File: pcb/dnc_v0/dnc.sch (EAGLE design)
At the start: 17 parts, among them IC1 74HC595D, IC2 74HC595D, Q1 MOSFET-NCHANNEL_DUALFDMA1024NZ, U1 ATMEGA168, Y1 16MHZ

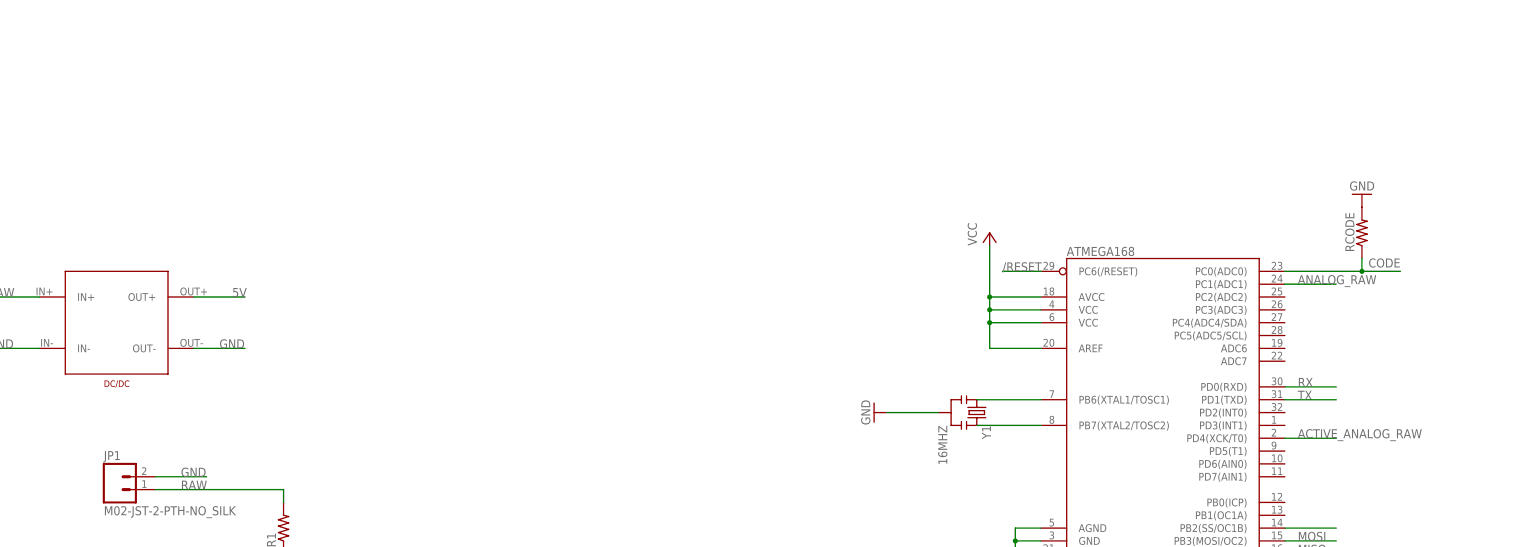
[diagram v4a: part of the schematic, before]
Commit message: Add Temp sensor and two 74HC595 for titreur select
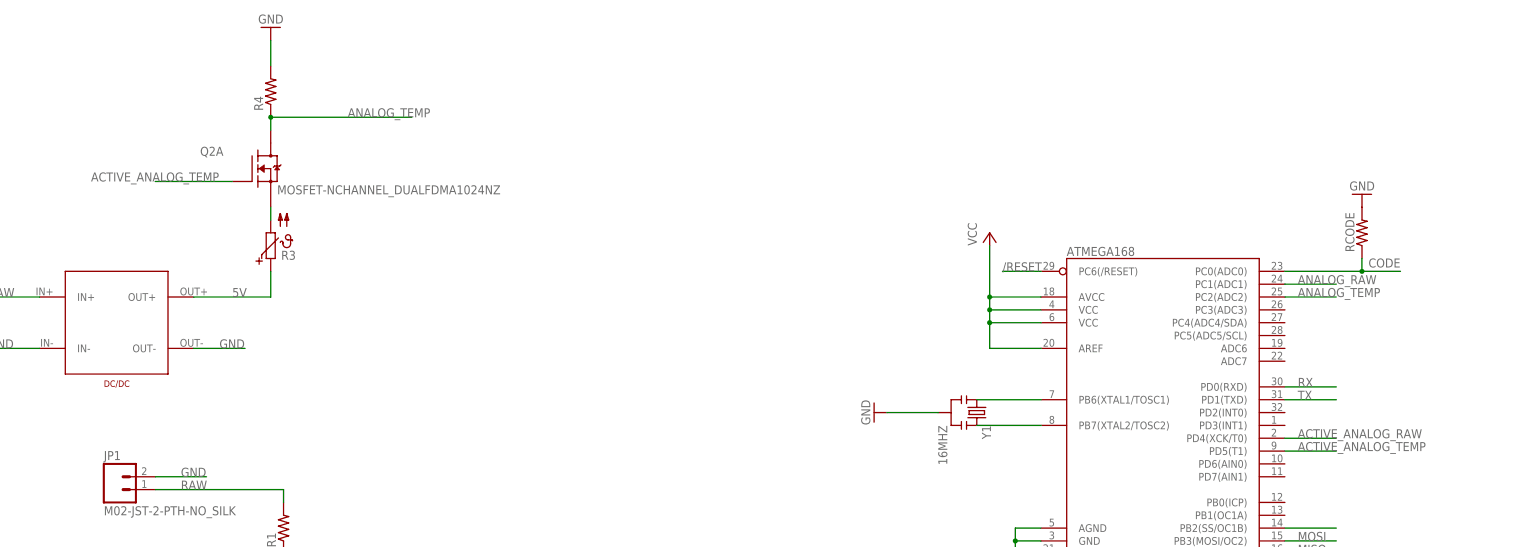
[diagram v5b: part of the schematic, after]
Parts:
- added Q2: MOSFET-NCHANNEL_DUALFDMA1024NZ, SparkFun-DiscreteSemi:MOSFET-NCHANNEL_DUALFDMA1024NZ
- added R3: (no value), ptc-ntc:PTC679
- added R4: (no value), SparkFun-Passives:RESISTOR1206
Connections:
- new net ACTIVE_ANALOG_TEMP: Q2A.G, U1.PD5(T1)
- new net ANALOG_TEMP: Q2A.D1, R4.1, U1.PC2(ADC2)
- new net N$11: Q2A.S, R3.2
- net 5V: now also R3.1
- net GND: now also R4.2
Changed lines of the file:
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@@
 <part name="U$7" library="pierre_vv" deviceset="EXT-DNC" device=""/>
 <part name="U$8" library="pierre_vv" deviceset="EXT-DNC" device=""/>
+<part name="R3" library="ptc-ntc" deviceset="PTC679" device=""/>
+<part name="R4" library="SparkFun-Passives" deviceset="RESISTOR" device="1206"/>
+<part name="GND3" library="SparkFun-Aesthetics" deviceset="GND" device=""/>
+<part name="Q2" library="SparkFun-DiscreteSemi" deviceset="MOSFET-NCHANNEL_DUAL" device="FDMA1024NZ"/>
 </parts>
 <sheets>
@@
 <instance part="U$7" gate="G$1" x="-45.72" y="-180.34"/>
 <instance part="U$8" gate="G$1" x="-45.72" y="-203.2"/>
+<instance part="R3" gate="1" x="-132.08" y="109.22"/>
+<instance part="R4" gate="G$1" x="-132.08" y="139.7" rot="R90"/>
+<instance part="GND3" gate="1" x="-132.08" y="152.4" rot="R180"/>
+<instance part="Q2" gate="A" x="-134.62" y="124.46"/>
 </instances>
 <busses>
@@
 <wire x1="-40.64" y1="-195.58" x2="-7.62" y2="-195.58" width="0.1524" layer="91"/>
 <label x="-15.24" y="-195.58" size="1.778" layer="95"/>
+</segment>
+<segment>
+<pinref part="R4" gate="G$1" pin="2"/>
+<pinref part="GND3" gate="1" pin="GND"/>
+<wire x1="-132.08" y1="144.78" x2="-132.08" y2="149.86" width="0.1524" layer="91"/>
 </segment>
 </net>
@@
 <segment>
 <pinref part="U$5" gate="G$1" pin="OUT+"/>
-<wire x1="-147.32" y1="99.06" x2="-137.16" y2="99.06" width="0.1524" layer="91"/>
+<wire x1="-147.32" y1="99.06" x2="-132.08" y2="99.06" width="0.1524" layer="91"/>
 <label x="-139.7" y="99.06" size="1.778" layer="95"/>
+<pinref part="R3" gate="1" pin="1"/>
+<wire x1="-132.08" y1="99.06" x2="-132.08" y2="104.14" width="0.1524" layer="91"/>
 </segment>
 </net>
@@
 </segment>
 </net>
+<net name="N$11" class="0">
+<segment>
+<pinref part="R3" gate="1" pin="2"/>
+<pinref part="Q2" gate="A" pin="S"/>
+<wire x1="-132.08" y1="114.3" x2="-132.08" y2="116.84" width="0.1524" layer="91"/>
+</segment>
+</net>
+<net name="ANALOG_TEMP" class="0">
+<segment>
+<pinref part="Q2" gate="A" pin="D1"/>
+<pinref part="R4" gate="G$1" pin="1"/>
+<wire x1="-132.08" y1="132.08" x2="-132.08" y2="134.62" width="0.1524" layer="91"/>
+<wire x1="-132.08" y1="134.62" x2="-104.14" y2="134.62" width="0.1524" layer="91"/>
+<junction x="-132.08" y="134.62"/>
+<label x="-116.84" y="134.62" size="1.778" layer="95"/>
+</segment>
+<segment>
+<pinref part="U1" gate="G$1" pin="PC2(ADC2)"/>
+<wire x1="68.58" y1="99.06" x2="78.74" y2="99.06" width="0.1524" layer="91"/>
+<label x="71.12" y="99.06" size="1.778" layer="95"/>
+</segment>
+</net>
+<net name="ACTIVE_ANALOG_TEMP" class="0">
+<segment>
+<pinref part="Q2" gate="A" pin="G"/>
+<wire x1="-139.7" y1="121.92" x2="-154.94" y2="121.92" width="0.1524" layer="91"/>
+<label x="-167.64" y="121.92" size="1.778" layer="95"/>
+</segment>
+<segment>
+<pinref part="U1" gate="G$1" pin="PD5(T1)"/>
+<wire x1="68.58" y1="68.58" x2="78.74" y2="68.58" width="0.1524" layer="91"/>
+<label x="71.12" y="68.58" size="1.778" layer="95"/>
+</segment>
+</net>

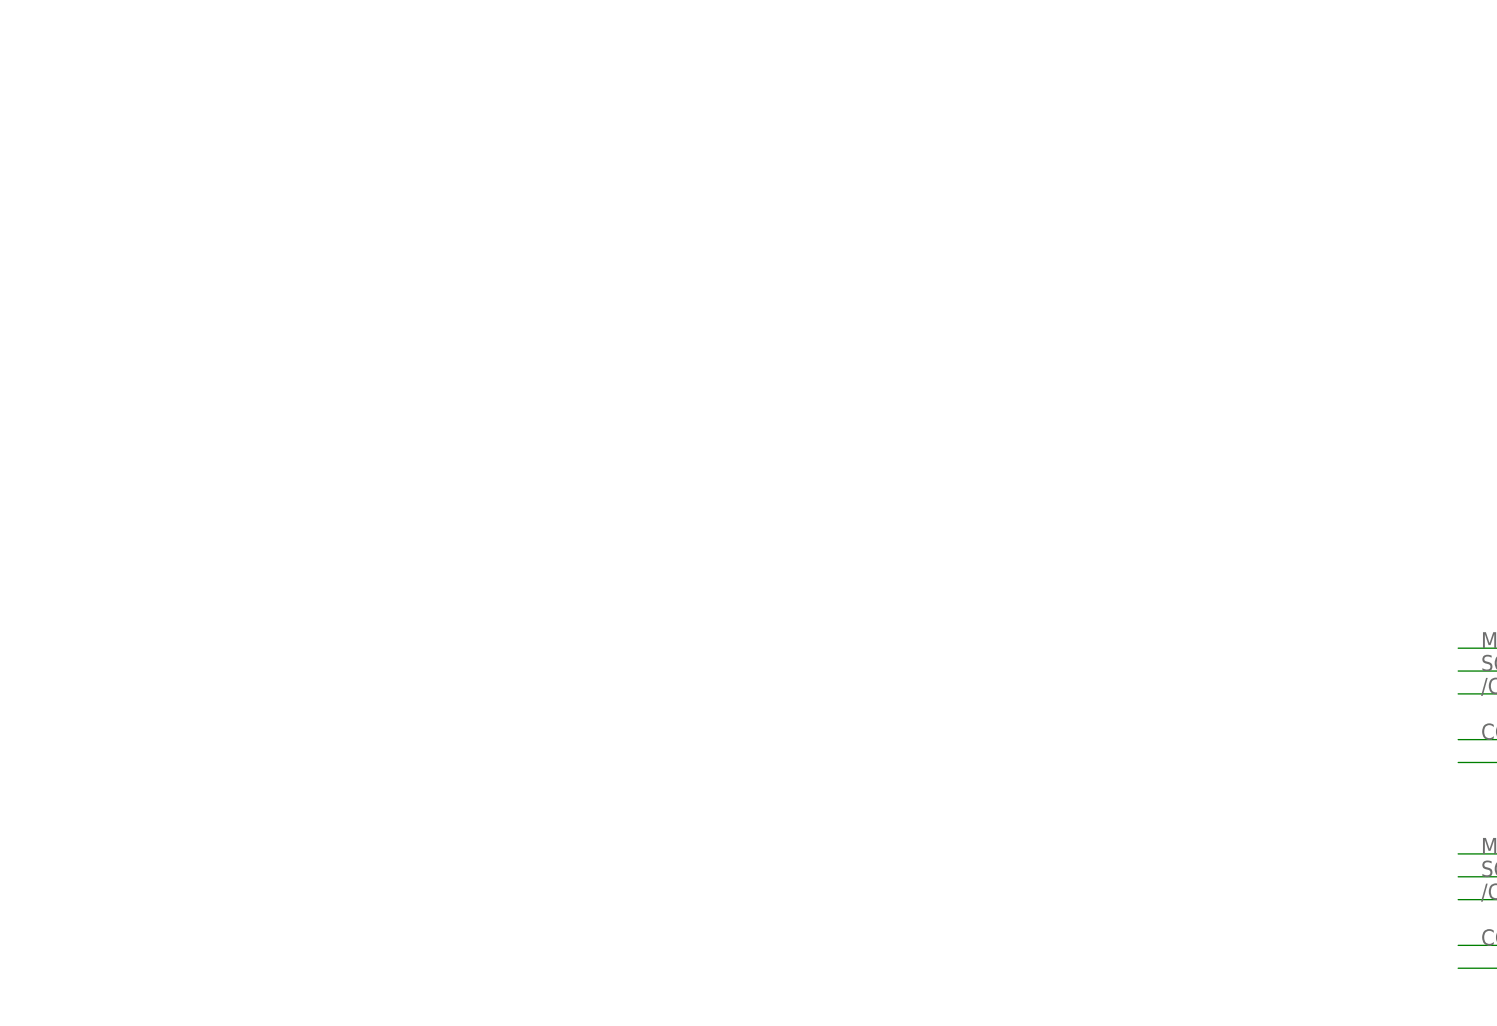
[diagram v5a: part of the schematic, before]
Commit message: Add 3 power output (ugly)
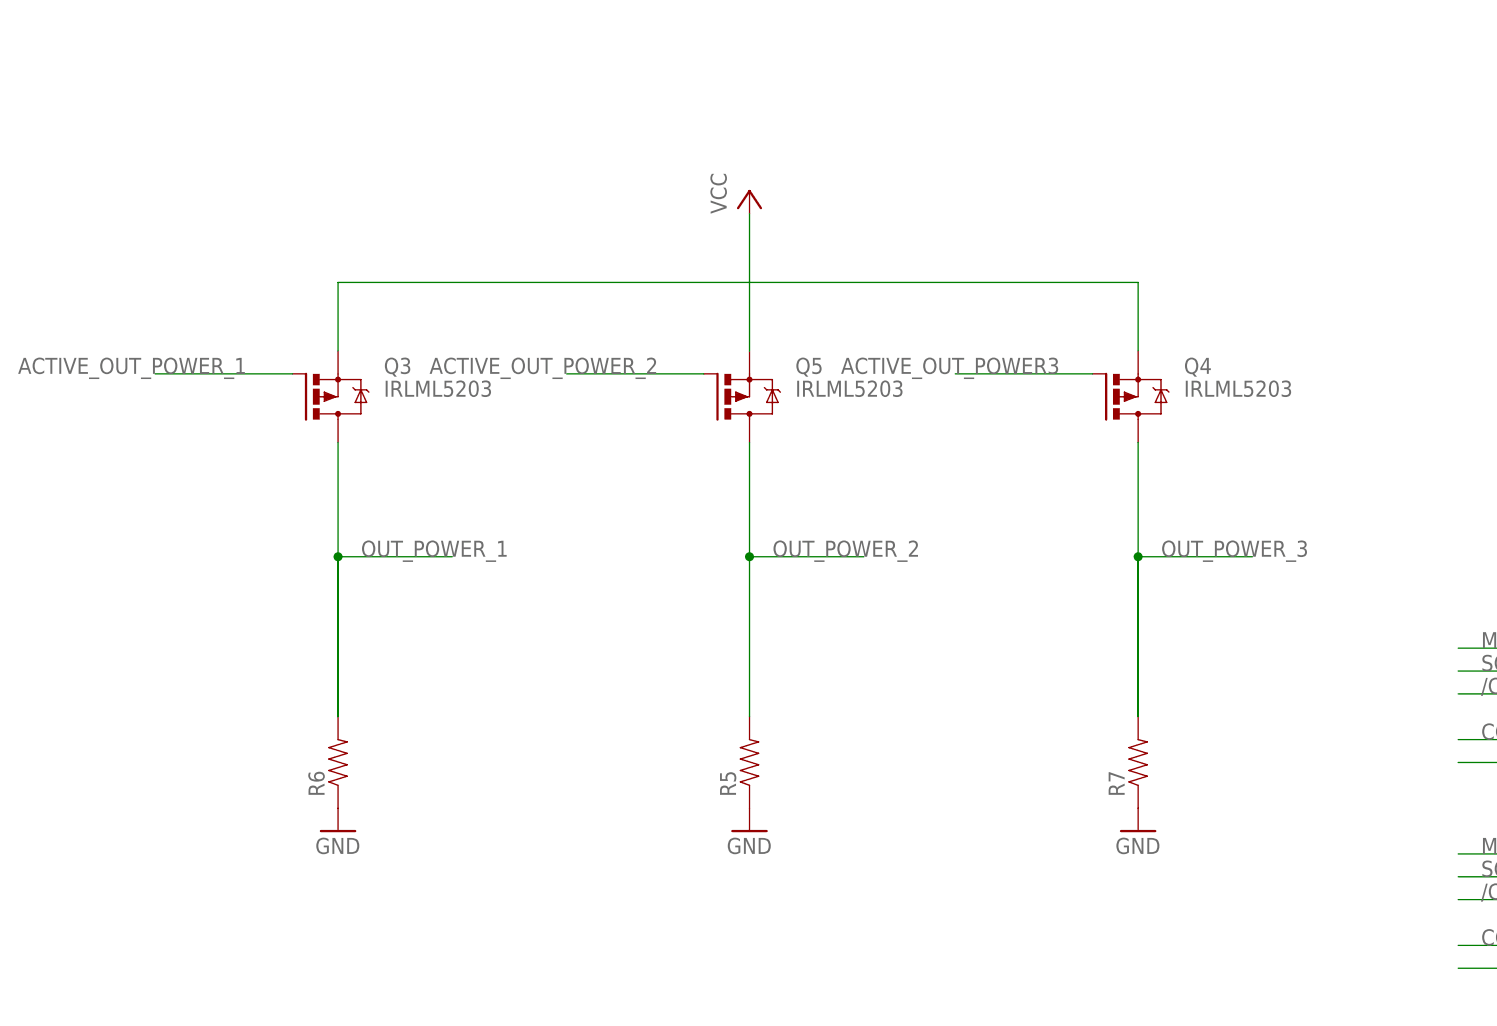
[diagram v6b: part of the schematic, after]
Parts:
- added Q3, Q4, Q5: IRLML5203, transistor-power:IRLML5203
- added R5, R6, R7: (no value), SparkFun-Passives:RESISTOR1206
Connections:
- new net ACTIVE_OUT_POWER3: Q4.G
- new net ACTIVE_OUT_POWER_1: Q3.G
- new net ACTIVE_OUT_POWER_2: Q5.G
- new net N$12: Q3.S, Q4.S
- new net N$26: R6.2
- new net N$29: R7.2
- new net OUT_POWER_1: Q3.D
- new net OUT_POWER_2: Q5.D, R5.2
- new net OUT_POWER_3: Q4.D
- net GND: now also R5.1, R6.1, R7.1
- net VCC: now also Q5.S
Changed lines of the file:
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@@
 <part name="GND3" library="SparkFun-Aesthetics" deviceset="GND" device=""/>
 <part name="Q2" library="SparkFun-DiscreteSemi" deviceset="MOSFET-NCHANNEL_DUAL" device="FDMA1024NZ"/>
+<part name="Q3" library="transistor-power" deviceset="IRLML5203" device=""/>
+<part name="Q4" library="transistor-power" deviceset="IRLML5203" device=""/>
+<part name="Q5" library="transistor-power" deviceset="IRLML5203" device=""/>
+<part name="R5" library="SparkFun-Passives" deviceset="RESISTOR" device="1206"/>
+<part name="GND4" library="SparkFun-Aesthetics" deviceset="GND" device=""/>
+<part name="P+3" library="supply1" deviceset="VCC" device=""/>
+<part name="R6" library="SparkFun-Passives" deviceset="RESISTOR" device="1206"/>
+<part name="GND7" library="SparkFun-Aesthetics" deviceset="GND" device=""/>
+<part name="R7" library="SparkFun-Passives" deviceset="RESISTOR" device="1206"/>
+<part name="GND8" library="SparkFun-Aesthetics" deviceset="GND" device=""/>
 </parts>
 <sheets>
@@
 <instance part="GND3" gate="1" x="-132.08" y="152.4" rot="R180"/>
 <instance part="Q2" gate="A" x="-134.62" y="124.46"/>
+<instance part="Q3" gate="G$1" x="-218.44" y="-48.26"/>
+<instance part="Q4" gate="G$1" x="-129.54" y="-48.26"/>
+<instance part="Q5" gate="G$1" x="-172.72" y="-48.26"/>
+<instance part="R5" gate="G$1" x="-170.18" y="-88.9" rot="R90"/>
+<instance part="GND4" gate="1" x="-170.18" y="-96.52"/>
+<instance part="P+3" gate="VCC" x="-170.18" y="-25.4"/>
+<instance part="R6" gate="G$1" x="-215.9" y="-88.9" rot="R90"/>
+<instance part="GND7" gate="1" x="-215.9" y="-96.52"/>
+<instance part="R7" gate="G$1" x="-127" y="-88.9" rot="R90"/>
+<instance part="GND8" gate="1" x="-127" y="-96.52"/>
 </instances>
 <busses>
@@
 <pinref part="GND3" gate="1" pin="GND"/>
 <wire x1="-132.08" y1="144.78" x2="-132.08" y2="149.86" width="0.1524" layer="91"/>
+</segment>
+<segment>
+<pinref part="R5" gate="G$1" pin="1"/>
+<pinref part="GND4" gate="1" pin="GND"/>
+</segment>
+<segment>
+<pinref part="R6" gate="G$1" pin="1"/>
+<pinref part="GND7" gate="1" pin="GND"/>
+</segment>
+<segment>
+<pinref part="R7" gate="G$1" pin="1"/>
+<pinref part="GND8" gate="1" pin="GND"/>
 </segment>
 </net>
@@
 <label x="-15.24" y="-190.5" size="1.778" layer="95"/>
 </segment>
+<segment>
+<pinref part="P+3" gate="VCC" pin="VCC"/>
+<pinref part="Q5" gate="G$1" pin="S"/>
+<wire x1="-170.18" y1="-43.18" x2="-170.18" y2="-27.94" width="0.1524" layer="91"/>
+</segment>
 </net>
 <net name="MOSI" class="0">
@@
 </segment>
 </net>
+<net name="N$12" class="0">
+<segment>
+<pinref part="Q3" gate="G$1" pin="S"/>
+<wire x1="-215.9" y1="-43.18" x2="-215.9" y2="-35.56" width="0.1524" layer="91"/>
+<wire x1="-215.9" y1="-35.56" x2="-127" y2="-35.56" width="0.1524" layer="91"/>
+<pinref part="Q4" gate="G$1" pin="S"/>
+<wire x1="-127" y1="-35.56" x2="-127" y2="-43.18" width="0.1524" layer="91"/>
+</segment>
+</net>
+<net name="OUT_POWER_1" class="0">
+<segment>
+<pinref part="Q3" gate="G$1" pin="D"/>
+<wire x1="-215.9" y1="-53.34" x2="-215.9" y2="-66.04" width="0.1524" layer="91"/>
+<wire x1="-215.9" y1="-66.04" x2="-215.9" y2="-83.82" width="0.1524" layer="91"/>
+<junction x="-215.9" y="-66.04"/>
+<wire x1="-215.9" y1="-66.04" x2="-203.2" y2="-66.04" width="0.1524" layer="91"/>
+<label x="-213.36" y="-66.04" size="1.778" layer="95"/>
+</segment>
+</net>
+<net name="ACTIVE_OUT_POWER_1" class="0">
+<segment>
+<pinref part="Q3" gate="G$1" pin="G"/>
+<wire x1="-220.98" y1="-45.72" x2="-236.22" y2="-45.72" width="0.1524" layer="91"/>
+<label x="-251.46" y="-45.72" size="1.778" layer="95"/>
+</segment>
+</net>
+<net name="ACTIVE_OUT_POWER_2" class="0">
+<segment>
+<pinref part="Q5" gate="G$1" pin="G"/>
+<wire x1="-175.26" y1="-45.72" x2="-190.5" y2="-45.72" width="0.1524" layer="91"/>
+<label x="-205.74" y="-45.72" size="1.778" layer="95"/>
+</segment>
+</net>
+<net name="ACTIVE_OUT_POWER3" class="0">
+<segment>
+<pinref part="Q4" gate="G$1" pin="G"/>
+<wire x1="-132.08" y1="-45.72" x2="-147.32" y2="-45.72" width="0.1524" layer="91"/>
+<label x="-160.02" y="-45.72" size="1.778" layer="95"/>
+</segment>
+</net>
+<net name="OUT_POWER_2" class="0">
+<segment>
+<pinref part="R5" gate="G$1" pin="2"/>
+<pinref part="Q5" gate="G$1" pin="D"/>
+<wire x1="-170.18" y1="-53.34" x2="-170.18" y2="-66.04" width="0.1524" layer="91"/>
+<wire x1="-170.18" y1="-66.04" x2="-157.48" y2="-66.04" width="0.1524" layer="91"/>
+<junction x="-170.18" y="-66.04"/>
+<wire x1="-170.18" y1="-66.04" x2="-170.18" y2="-83.82" width="0.1524" layer="91"/>
+<label x="-167.64" y="-66.04" size="1.778" layer="95"/>
+</segment>
+</net>
+<net name="N$26" class="0">
+<segment>
+<pinref part="R6" gate="G$1" pin="2"/>
+<wire x1="-215.9" y1="-66.04" x2="-215.9" y2="-83.82" width="0.1524" layer="91"/>
+</segment>
+</net>
+<net name="N$29" class="0">
+<segment>
+<pinref part="R7" gate="G$1" pin="2"/>
+<wire x1="-127" y1="-66.04" x2="-127" y2="-83.82" width="0.1524" layer="91"/>
+</segment>
+</net>
+<net name="OUT_POWER_3" class="0">
+<segment>
+<pinref part="Q4" gate="G$1" pin="D"/>
+<wire x1="-127" y1="-83.82" x2="-127" y2="-66.04" width="0.1524" layer="91"/>
+<wire x1="-127" y1="-66.04" x2="-127" y2="-53.34" width="0.1524" layer="91"/>
+<wire x1="-127" y1="-66.04" x2="-114.3" y2="-66.04" width="0.1524" layer="91"/>
+<junction x="-127" y="-66.04"/>
+<label x="-124.46" y="-66.04" size="1.778" layer="95"/>
+</segment>
+</net>

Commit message: Add 4 digital input and 3 analog input
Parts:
- added RANA1, RANA2, RANA3, RIN1, RIN2, RIN3, RIN4: (no value), SparkFun-Passives:RESISTOR2512
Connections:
- removed net ACTIVE_OUT_POWER3: Q4.G
- removed net N$13: U$4.GPIO2
- removed net N$14: U$4.GPIO3
- removed net N$16: U$4.GPIO17
- removed net N$17: U$4.GPIO27
- removed net N$41: U$4.GPIO16
- removed net N$42: U$4.GPIO20
- removed net N$43: U$4.GPIO21
- new net ACTIVE_OUT_POWER_3: Q4.G, U$4.GPIO21
- new net ANALOG_IN_1: RANA1.2, U1.PC3(ADC3)
- new net ANALOG_IN_2: RANA2.2, U1.PC4(ADC4/SDA)
- new net ANALOG_IN_3: RANA3.2, U1.PC5(ADC5/SCL)
- new net IN_1: RIN1.2, U$4.GPIO2
- new net IN_2: RIN2.2, U$4.GPIO3
- new net IN_3: RIN3.2, U$4.GPIO17
- new net IN_4: RIN4.2, U$4.GPIO27
- net ACTIVE_OUT_POWER_1: now also U$4.GPIO16
- net ACTIVE_OUT_POWER_2: now also U$4.GPIO20
- net GND: now also RANA1.1, RANA2.1, RANA3.1, RIN1.1, RIN2.1, RIN3.1, RIN4.1

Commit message: Correct MOSFET
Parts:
- removed Q5: IRLML5203, transistor-power:IRLML5203
- added Q6: 200mA/50V, SparkFun-DiscreteSemi:MOSFET-NCHANNELBSS138
- added R8: 100K, SparkFun-Passives:RESISTOR1206
- Q1: value MOSFET-NCHANNEL_DUALFDMA1024NZ -> 200mA/50V; device SparkFun-DiscreteSemi:MOSFET-NCHANNEL_DUALFDMA1024NZ -> SparkFun-DiscreteSemi:MOSFET-NCHANNELBSS138
- Q2: value MOSFET-NCHANNEL_DUALFDMA1024NZ -> TSM2306CX; device SparkFun-DiscreteSemi:MOSFET-NCHANNEL_DUALFDMA1024NZ -> SparkFun-DiscreteSemi:MOSFET-NCHANNEL2N7002PW
- Q3, Q4: value IRLML5203 -> TSM2306CX; device transistor-power:IRLML5203 -> SparkFun-DiscreteSemi:MOSFET-NCHANNEL2N7002PW
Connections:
- removed net N$12: Q3.S, Q4.S
- removed net N$6: U1.PB2(SS/OC1B)
- removed net OUT_POWER_3: Q4.D
- new net ATMEGA_CS: U$4.GND_4, U1.PB2(SS/OC1B)
- net ACTIVE_ANALOG_RAW: now also Q1.G, R8.2; no longer Q1A.G
- net ACTIVE_ANALOG_TEMP: now also Q6.G; no longer Q2A.G
- net ACTIVE_OUT_POWER_2: now also Q2.G; no longer Q5.G
- net ANALOG_RAW: now also Q1.S; no longer Q1A.S
- net ANALOG_TEMP: now also Q6.S; no longer Q2A.D1
- net GND: now also R8.1; no longer U$4.GND_4
- net N$11: now also Q6.D; no longer Q2A.S
- net N$29: now also Q4.S
- net N$3: now also Q1.D; no longer Q1A.D1
- net OUT_POWER_1: now also Q3.S; no longer Q3.D
- net OUT_POWER_2: now also Q2.S; no longer Q5.D
- net VCC: now also Q2.D, Q3.D, Q4.D; no longer Q5.S
